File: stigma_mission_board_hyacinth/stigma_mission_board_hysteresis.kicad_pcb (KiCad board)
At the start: 4 copper layers, 85.8 x 120 mm, 190 parts, among them J1 DF40C-70DS-0.4V(51), J10 JST-GH, J2 DF40HB(2.5)-10DS-0.4V(51), J6 SMA, J7 SMA, J8 RJ45_Wuerth_7499010211A, J9 JST-GH, Q1 TPH1R712MD, Q2 AO3400A, Q3 AO3401A, Q4 AO3400A, Q5 TPH4R008NH, Q6 TPH4R008NH, Q7 TPH4R008NH, Q8 TPH4R008NH, U1 L7805, U10 MCP2562, U11 Ai-Thinker-Ra-01, U12 TPD4E1U06, U13 Ai-Thinker-Ra-01, U14 LAN8742A, U15 TF0216, U16 TF0216, U17 TF0216, U18 TF0216, U2 AZ1117I-3.3, U3 AZ1117I-3.3, U4 INA181A4, U5 L7805, U6 AZ1117I-3.3, U7 AZ1117I-3.3, U8 MCP2562, U9 INA181A4, Y1 25MHz

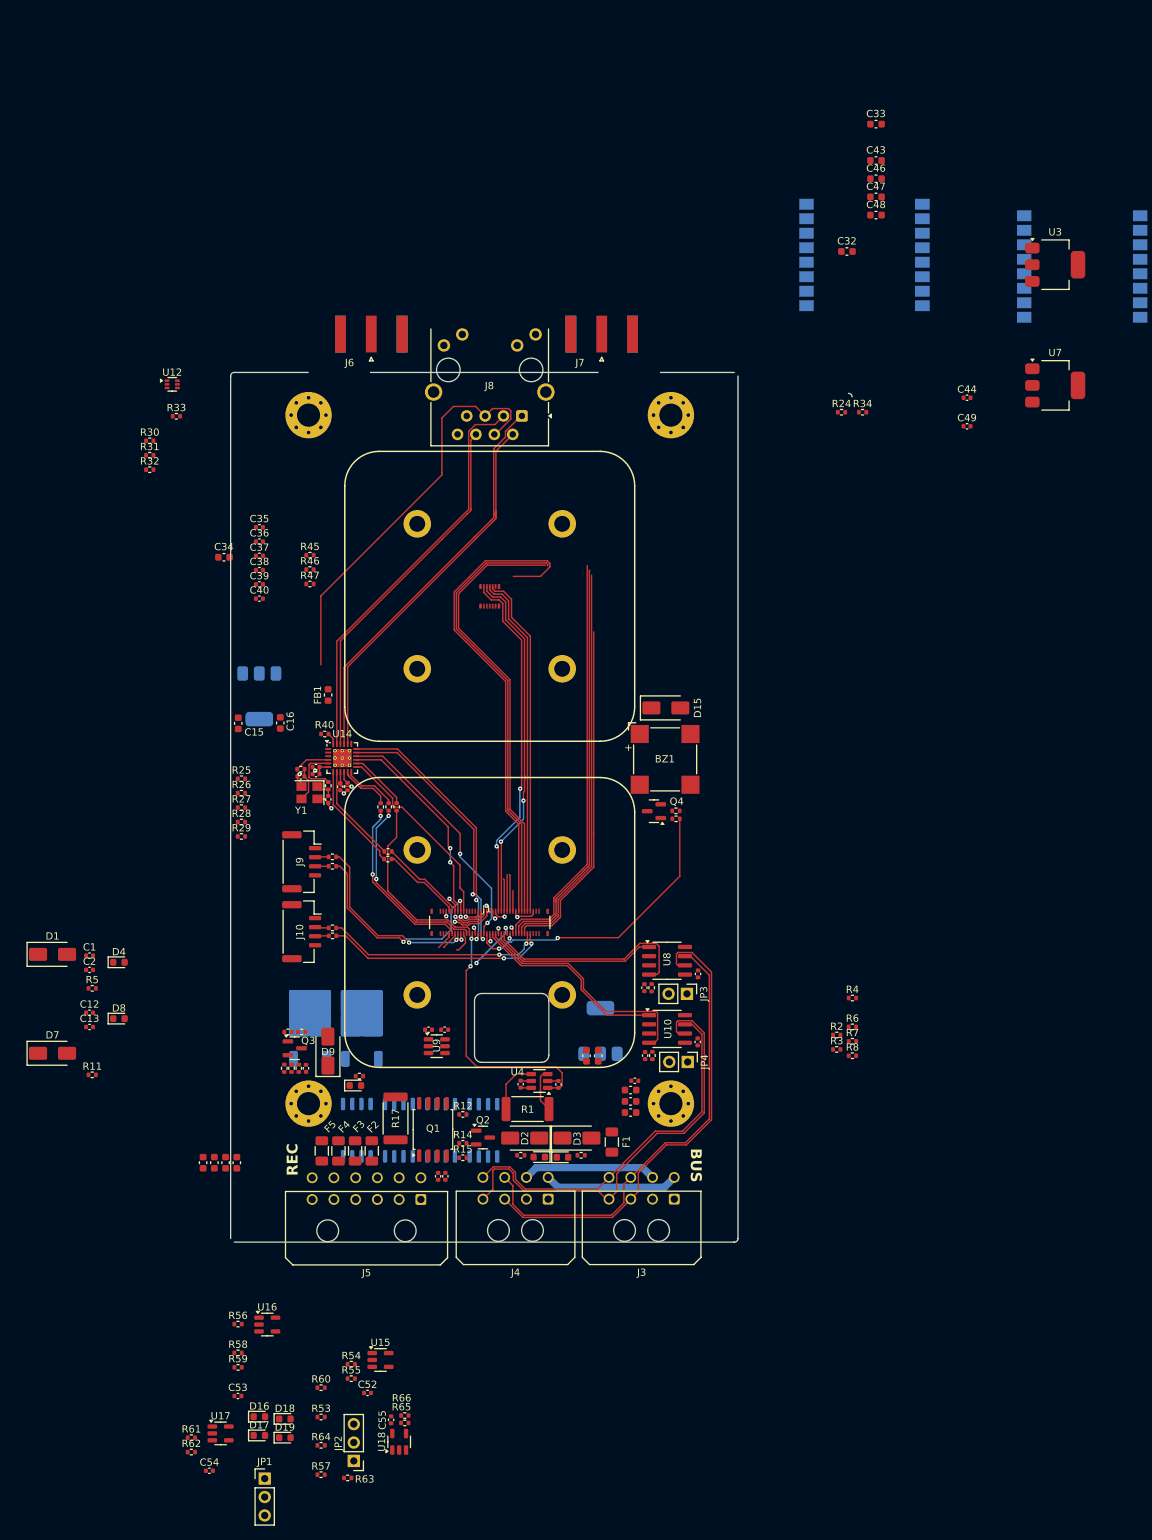
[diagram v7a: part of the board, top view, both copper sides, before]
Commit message: progress on routing, add some 3d models
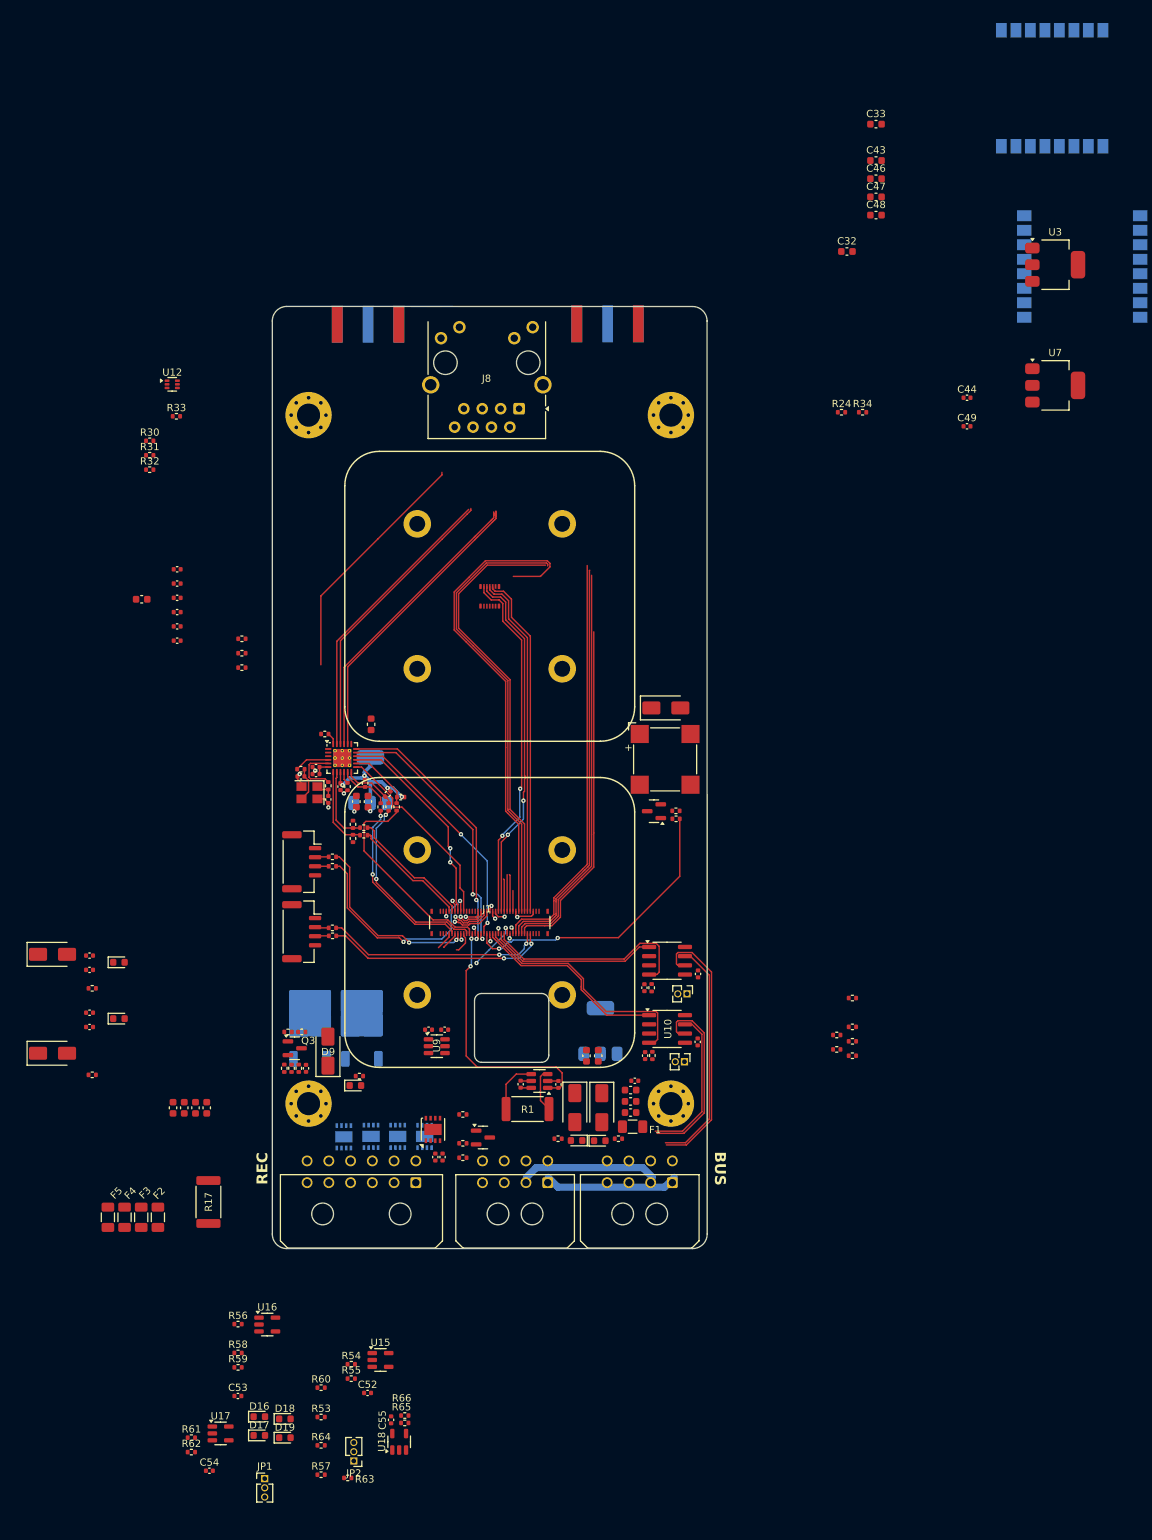
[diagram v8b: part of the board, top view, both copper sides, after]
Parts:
- J6, J7: moved to B.Cu
- JP1, JP2: footprint Connector_PinHeader_2.54mm:PinHeader_1x03_P2.54mm_Vertical -> Connector_PinHeader_1.27mm:PinHeader_1x03_P1.27mm_Vertical
- JP3, JP4: footprint Connector_PinHeader_2.54mm:PinHeader_1x02_P2.54mm_Vertical -> Connector_PinHeader_1.27mm:PinHeader_1x02_P1.27mm_Vertical
- Q1, Q5, Q6, Q7, Q8: footprint Package_SO:SSOP-8_5.25x5.24mm_P1.27mm -> Package_DFN_QFN:DFN-8-1EP_3x3mm_P0.65mm_EP1.55x2.4mm
- moved U11 34.6 mm to (277.6, 84.9), turned to -90 degrees
- moved F3 30.9 mm to (151.9, 240.7)
- moved F2 30.9 mm to (154.2, 240.7)
- moved F4 30.9 mm to (149.6, 240.7)
- moved F5 30.9 mm to (147.3, 240.7)
- moved R17 28.3 mm to (161.2, 238.6)
- moved R25 22.1 mm to (187.7, 182.7)
- moved R26 20.2 mm to (185.9, 182.3), turned to 45 degrees
- moved C15 19.6 mm to (181.6, 183.3), turned to -90 degrees
- moved U6 19.2 mm to (183.5, 180.4), turned to 90 degrees
- moved R27 17.4 mm to (182.8, 180.8), turned to 90 degrees
- moved C16 16.3 mm to (183.2, 183.3)
- moved R28 15.6 mm to (181.1, 188.4), turned to -90 degrees
- moved R29 15.5 mm to (181.1, 186.5), turned to 90 degrees
- moved R45 14.9 mm to (165.8, 160.9)
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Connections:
- net /Recovery Output Pair 1/out1_high renamed R1_H
- net /Recovery Output Pair 1/out2_low renamed R2_L
- net /Recovery Output Pair 2/out1_high renamed R3_H
- net /Recovery Output Pair 2/out2_low renamed R4_L
- D16 pad 1: /Recovery Output Pair 1/out1_low -> R2_H
- D18 pad 1: /Recovery Output Pair 2/out1_low -> R4_H
- J5 pad 10: /Recovery Output Pair 1/out2_high -> R2_H
- J5 pad 12: /Recovery Output Pair 2/out2_high -> R4_H
- J5 pad 3: /Recovery Output Pair 1/out1_low -> R1_L
- J5 pad 5: /Recovery Output Pair 2/out1_low -> R3_L
- JP1 pad 2: /Recovery Output Pair 1/out2_high -> R1_L
- JP2 pad 2: /Recovery Output Pair 2/out2_high -> R3_L
- Q5 pad 5: /Recovery Output Pair 1/out1_low -> R2_H
- Q7 pad 5: /Recovery Output Pair 2/out1_low -> R4_H
- R57 pad 1: /Recovery Output Pair 1/out2_high -> R1_L
- R64 pad 1: /Recovery Output Pair 2/out2_high -> R3_L
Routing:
- net CAN2-: track 60.7 -> 25.9 mm
- net CAN1+: track 63.2 -> 31.7 mm
- net CAN2+: track 50.7 -> 21.1 mm
- net CAN1-: track 65.7 -> 36.7 mm
- net Net-(J8-CRD): track 56.5 -> 33.5 mm
- net vdd_ethernet: track 3.55 -> 23.3 mm, vias 1 -> 5
- net /RXP: track 56.4 -> 39.9 mm
- net /TXP: track 55.5 -> 40.6 mm
- net /TXN: track 52.2 -> 40.6 mm
- net /RXN: track 50.6 -> 39.9 mm
- net ETH_RXD-: track 12.1 -> 17.4 mm
- net ETH_RXD+: track 11.3 -> 16.2 mm
- net Net-(U14-RXD1/MODE1): track 14.9 -> 11.4 mm
- net Net-(U14-RXD0/MODE0): track 13.7 -> 10.5 mm
- net ETH_REF_CLK: track 25.7 -> 28.8 mm
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- removed copper zone on In1.Cu, net GND
- removed copper zone on In2.Cu, net GND
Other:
- board size 85.8 x 120 mm -> 60 x 130 mm
